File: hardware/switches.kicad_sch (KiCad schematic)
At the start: 63 parts, among them SW1 SW_SPST, SW2 SW_SPST, SW3 SW_SPST, SW4 SW_SPST, SW5 SW_SPST, SW6 SW_SPST, SW7 SW_SPST

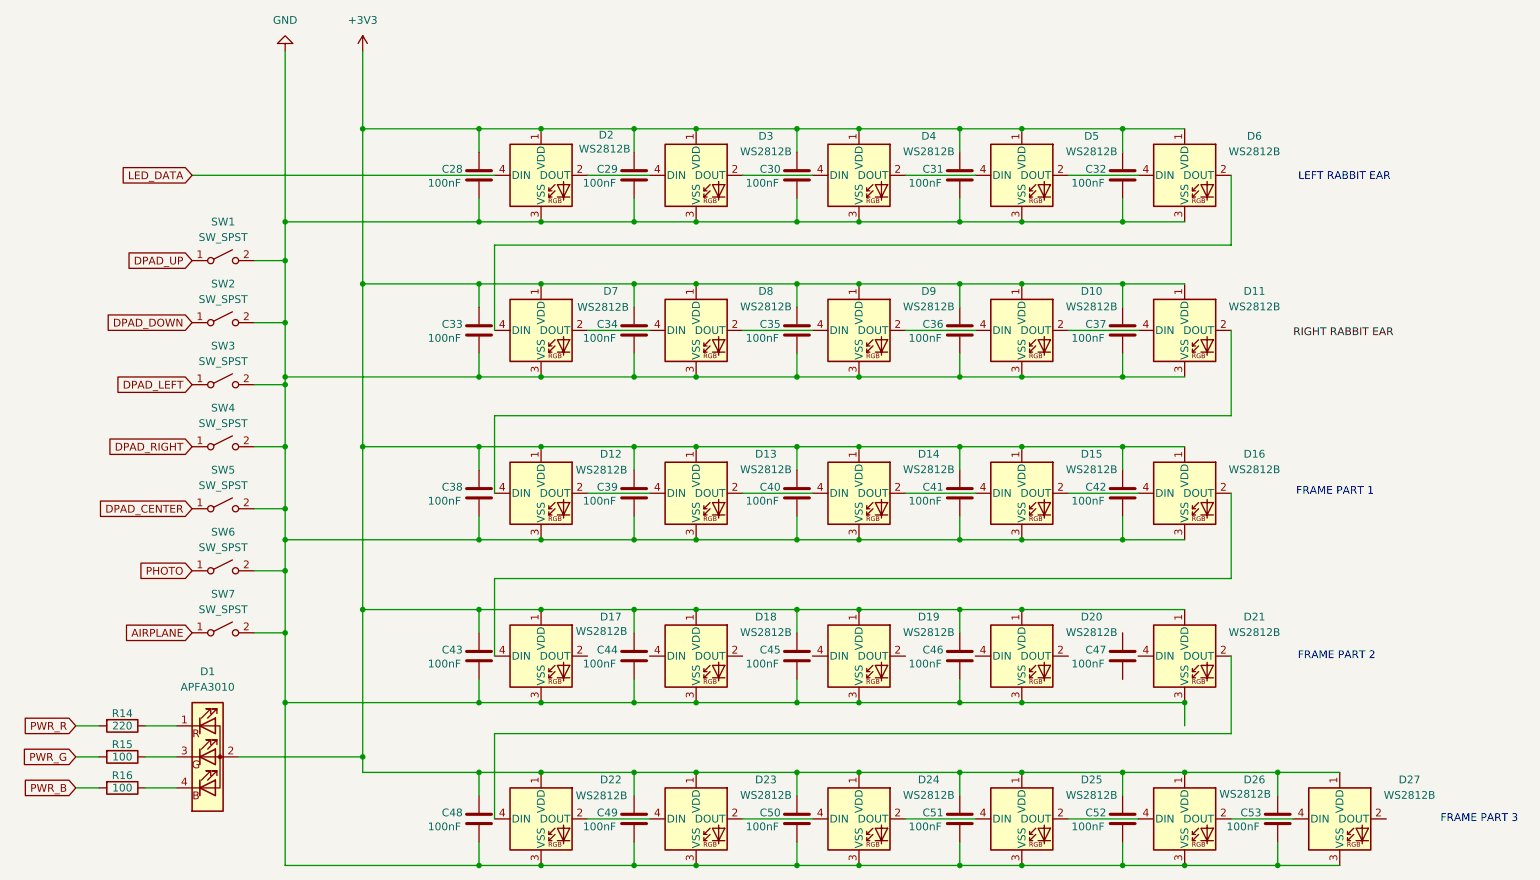
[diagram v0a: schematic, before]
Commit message: all design sheets complete, ERC clean
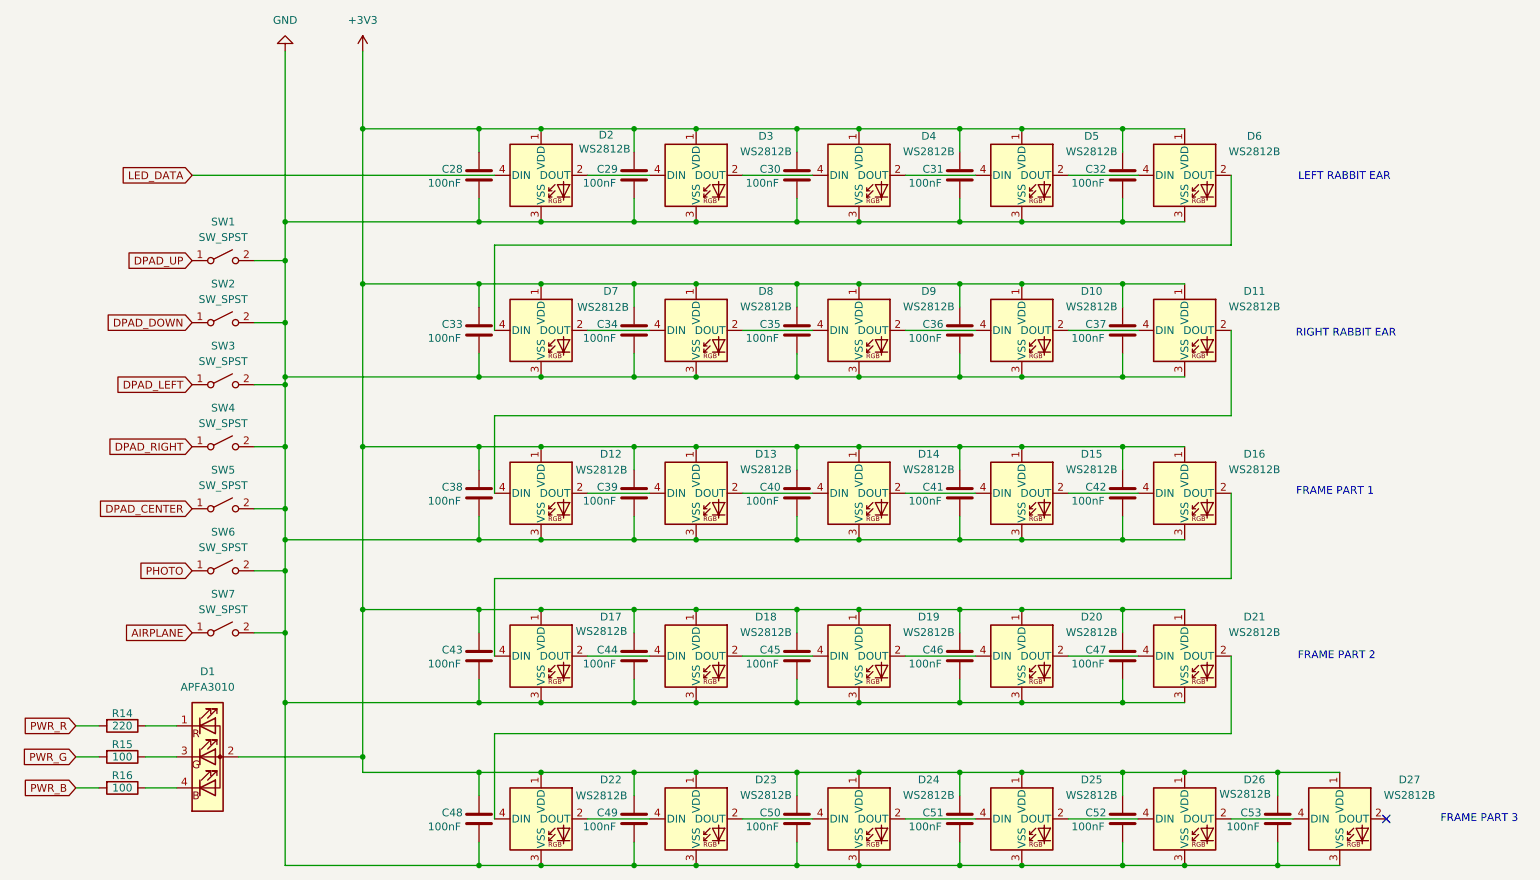
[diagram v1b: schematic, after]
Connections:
- net +3V3: now also C47.1
- net GND: now also C47.2
- net at D19.2 (DOUT): now also D20.4 (DIN)
- net at D19.4 (DIN): now also D18.2 (DOUT)
- net at D21.4 (DIN): now also D20.2 (DOUT)
- net at D17.2 (DOUT): now also D18.4 (DIN)
- no-connect marks 0 -> 1
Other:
- note added: "RIGHT RABBIT EAR"
